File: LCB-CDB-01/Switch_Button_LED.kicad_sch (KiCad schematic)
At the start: 65 parts, among them J1 Conn_01x02, J10 Conn_01x02, J11 Conn_01x02, J12 Conn_01x02, J13 Conn_01x02, J14 Conn_01x02, J15 Conn_01x02, J16 Conn_01x02, J17 Conn_01x02, J18 Conn_01x02, J19 Conn_01x02, J2 Conn_01x02, J20 Conn_01x02, J21 Conn_01x02, J22 Conn_01x02, J23 Conn_01x02, J24 Conn_01x02, J25 Conn_01x02, J26 Conn_01x02, J27 Conn_01x02, J28 Conn_01x02, J29 Conn_01x02, J3 Conn_01x02, J30 Conn_01x02, J4 Conn_01x02, J5 Conn_01x02, J6 Conn_01x02, J7 Conn_01x02, J8 Conn_01x02, J9 Conn_01x02

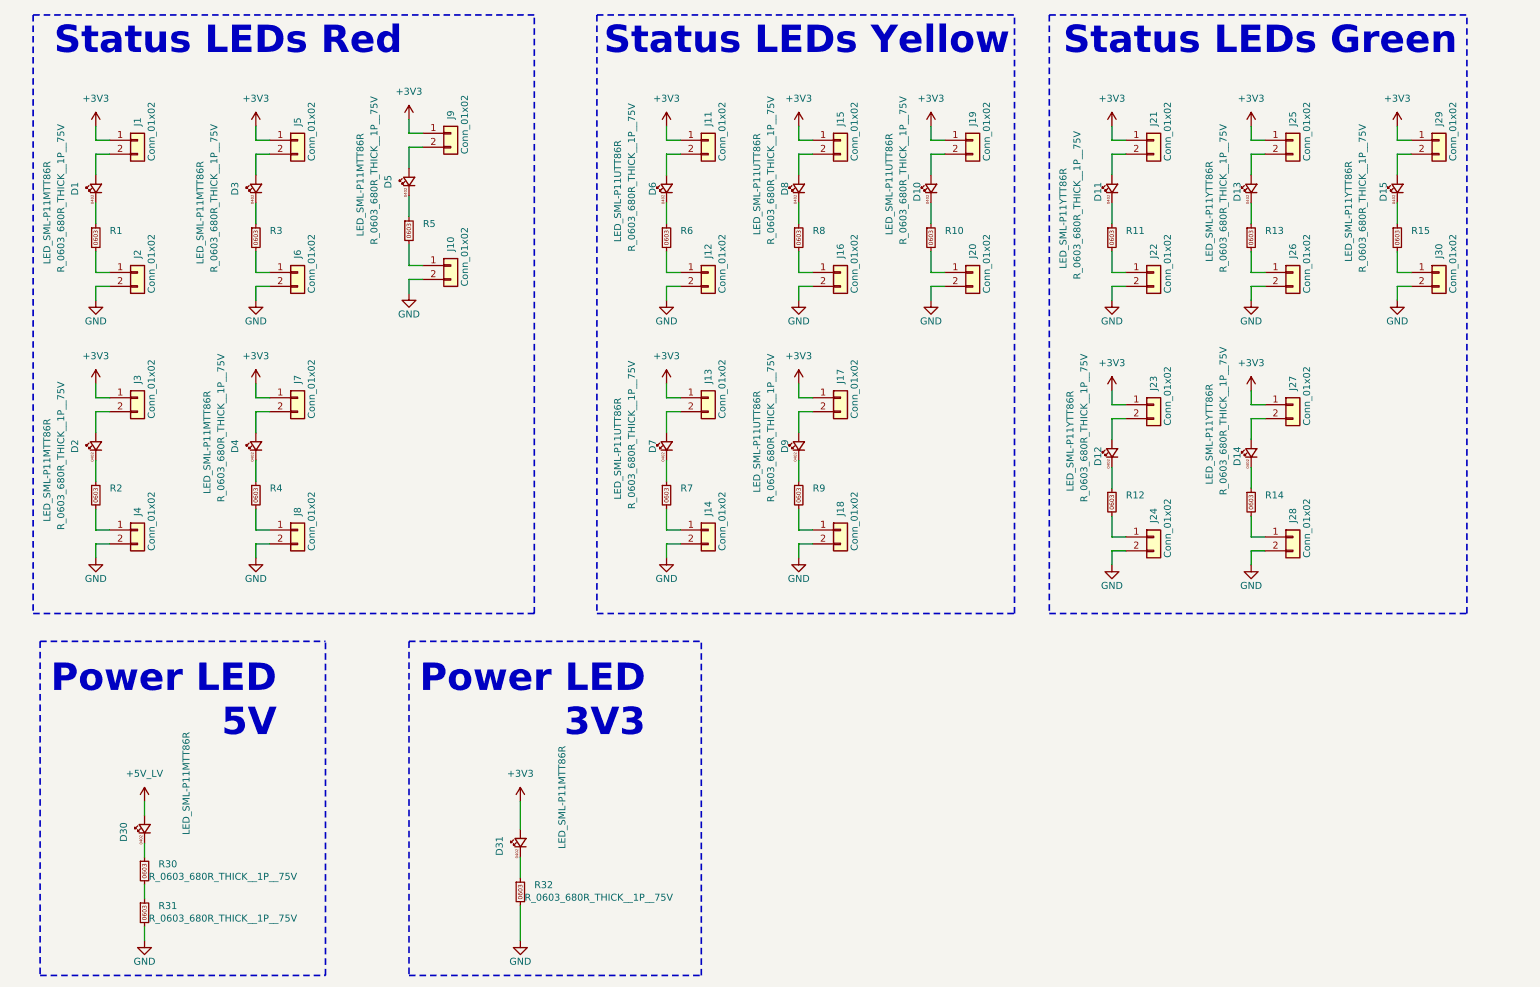
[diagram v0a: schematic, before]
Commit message: update some Rs and Cs names and values, as they can be separate values in KiCad7
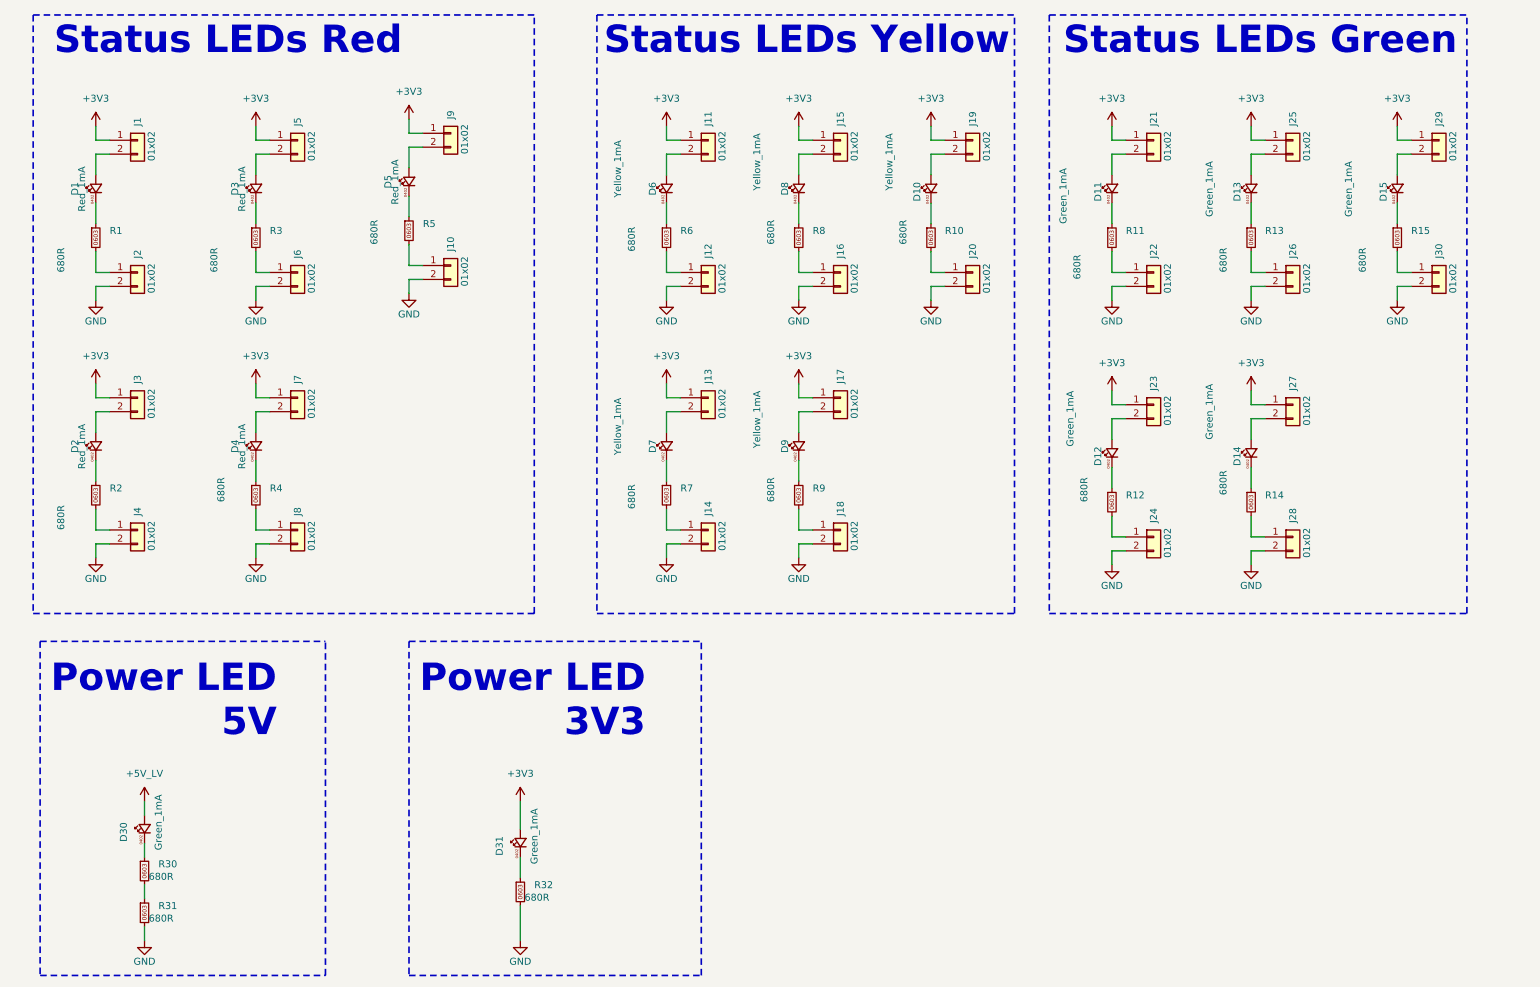
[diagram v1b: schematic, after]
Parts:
- D1, D2, D3, D4, D5: value LED_SML-P11MTT86R -> Red_1mA; symbol LEA_SymbolLibrary:LED_0402_Y_1mA_SML-P11YTT86R -> LEA_SymbolLibrary:LED_0402_R_1mA_SML-P11UTT86R; manf# SML-P11YTT86R -> SML-P11UTT86R; mouser# 755-SML-P11YTT86R -> 755-SML-P11UTT86R
- D10, D6, D7, D8, D9: value LED_SML-P11UTT86R -> Yellow_1mA
- D11, D12, D13, D14, D15: value LED_SML-P11YTT86R -> Green_1mA
- D30, D31: value LED_SML-P11MTT86R -> Green_1mA
- J1, J10, J11, J12, J13, J14, J15, J16, J17, J18, J19, J2, J20, J21, J22, J23, J24, J25, J26, J27, J28, J29, J3, J30, J4, J5, J6, J7, J8, J9: value Conn_01x02 -> 01x02
- R1, R10, R11, R12, R13, R14, R15, R2, R3, R30, R31, R32, R4, R5, R6, R7, R8, R9: value R_0603_680R_THICK__1P__75V -> 680R

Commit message: bump version to 1.1.0
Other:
- title: LCB-CBD-001: Dock -> LCB-CBD-01: Dock
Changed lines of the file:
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@@
   (paper "A4")
   (title_block
-    (title "LCB-CBD-001: Dock")
-    (date "2022-08-12")
-    (rev "0.1")
+    (title "LCB-CBD-01: Dock")
+    (date "2023-04-13")
+    (rev "1.1.0")
     (company "PADERBORN UNIVERSITY DEPARTMENT OF POWER ELECTRONICS AND ELECTRICAL DRIVES")
   )
@@
   (symbol (lib_id "LEA_SymbolLibrary:R_0603_680R_THICK__1P__75V") (at 135.89 55.88 0) (unit 1)
     (in_bom yes) (on_board yes) (dnp no)
-    (property "Reference" "R6" (at 138.43 54.61 0)
+    (property "Reference" "R6" (at 137.16 54.61 0)
       (effects (font (size 1.27 1.27)) (justify left))
     )
-    (property "Value" "680R" (at 129.54 58.42 90)
+    (property "Value" "680R" (at 133.35 58.42 90)
       (effects (font (size 1.27 1.27)) (justify left))
     )
@@
   (symbol (lib_id "LEA_SymbolLibrary:LED_0402_R_1mA_SML-P11UTT86R") (at 60.96 46.99 90) (unit 1)
     (in_bom yes) (on_board yes) (dnp no)
-    (property "Reference" "D3" (at 57.15 45.72 0)
+    (property "Reference" "D3" (at 55.88 45.72 0)
       (effects (font (size 1.27 1.27)) (justify right))
     )
@@
       (effects (font (size 1.27 1.27)) (justify left))
     )
-    (property "Value" "680R" (at 212.09 104.14 90)
+    (property "Value" "680R" (at 214.63 106.68 90)
       (effects (font (size 1.27 1.27)) (justify left))
     )
@@
   (symbol (lib_id "LEA_SymbolLibrary:LED_0402_R_1mA_SML-P11UTT86R") (at 60.96 93.98 90) (unit 1)
     (in_bom yes) (on_board yes) (dnp no)
-    (property "Reference" "D4" (at 57.15 92.71 0)
+    (property "Reference" "D4" (at 55.88 92.71 0)
       (effects (font (size 1.27 1.27)) (justify right))
     )
@@
       (effects (font (size 1.27 1.27)) (justify left))
     )
-    (property "Value" "680R" (at 262.89 62.23 90)
+    (property "Value" "680R" (at 266.7 58.42 90)
       (effects (font (size 1.27 1.27)) (justify left))
     )
@@
   (symbol (lib_id "LEA_SymbolLibrary:R_0603_680R_THICK__1P__75V") (at 31.75 102.87 0) (unit 1)
     (in_bom yes) (on_board yes) (dnp no)
-    (property "Reference" "R2" (at 34.29 101.6 0)
+    (property "Reference" "R2" (at 33.02 101.6 0)
       (effects (font (size 1.27 1.27)) (justify left))
     )
-    (property "Value" "680R" (at 25.4 109.22 90)
+    (property "Value" "680R" (at 29.21 105.41 90)
       (effects (font (size 1.27 1.27)) (justify left))
     )
@@
       (effects (font (size 1.27 1.27)) (justify right))
     )
-    (property "Value" "Green_1mA" (at 234.95 41.91 0)
+    (property "Value" "Green_1mA" (at 237.49 41.91 0)
       (effects (font (size 1.27 1.27)) (justify right))
     )
@@
   (symbol (lib_id "LEA_SymbolLibrary:LED_0402_R_1mA_SML-P11UTT86R") (at 31.75 46.99 90) (unit 1)
     (in_bom yes) (on_board yes) (dnp no)
-    (property "Reference" "D1" (at 27.94 45.72 0)
+    (property "Reference" "D1" (at 26.67 45.72 0)
       (effects (font (size 1.27 1.27)) (justify right))
     )
@@
       (effects (font (size 1.27 1.27)) (justify left))
     )
-    (property "Value" "680R" (at 237.49 62.23 90)
+    (property "Value" "680R" (at 240.03 58.42 90)
       (effects (font (size 1.27 1.27)) (justify left))
     )
@@
       (effects (font (size 1.27 1.27)) (justify right))
     )
-    (property "Value" "Yellow_1mA" (at 176.53 36.83 0)
+    (property "Value" "Yellow_1mA" (at 179.07 40.64 0)
       (effects (font (size 1.27 1.27)) (justify right))
     )
@@
       (effects (font (size 1.27 1.27)) (justify right))
     )
-    (property "Value" "Yellow_1mA" (at 127 38.1 0)
+    (property "Value" "Yellow_1mA" (at 130.81 41.91 0)
       (effects (font (size 1.27 1.27)) (justify right))
     )
@@
       (effects (font (size 1.27 1.27)) (justify right))
     )
-    (property "Value" "Yellow_1mA" (at 127 85.09 0)
+    (property "Value" "Yellow_1mA" (at 130.81 87.63 0)
       (effects (font (size 1.27 1.27)) (justify right))
     )
@@
       (effects (font (size 1.27 1.27)) (justify right))
     )
-    (property "Value" "Green_1mA" (at 208.28 43.18 0)
+    (property "Value" "Green_1mA" (at 212.09 43.18 0)
       (effects (font (size 1.27 1.27)) (justify right))
     )
@@
       (effects (font (size 1.27 1.27)) (justify right))
     )
-    (property "Value" "Yellow_1mA" (at 152.4 83.82 0)
+    (property "Value" "Yellow_1mA" (at 154.94 87.63 0)
       (effects (font (size 1.27 1.27)) (justify right))
     )
@@
   (symbol (lib_id "LEA_SymbolLibrary:R_0603_680R_THICK__1P__75V") (at 60.96 55.88 0) (unit 1)
     (in_bom yes) (on_board yes) (dnp no)
-    (property "Reference" "R3" (at 63.5 54.61 0)
+    (property "Reference" "R3" (at 62.23 55.88 0)
       (effects (font (size 1.27 1.27)) (justify left))
     )
-    (property "Value" "680R" (at 53.34 62.23 90)
+    (property "Value" "680R" (at 58.42 58.42 90)
       (effects (font (size 1.27 1.27)) (justify left))
     )
@@
       (effects (font (size 1.27 1.27)) (justify left))
     )
-    (property "Value" "680R" (at 179.07 57.15 90)
+    (property "Value" "680R" (at 181.61 58.42 90)
       (effects (font (size 1.27 1.27)) (justify left))
     )
@@
   (symbol (lib_id "LEA_SymbolLibrary:LED_0402_R_1mA_SML-P11UTT86R") (at 88.9 45.72 90) (unit 1)
     (in_bom yes) (on_board yes) (dnp no)
-    (property "Reference" "D5" (at 85.09 44.45 0)
+    (property "Reference" "D5" (at 83.82 44.45 0)
       (effects (font (size 1.27 1.27)) (justify right))
     )
@@
       (effects (font (size 1.27 1.27)) (justify left))
     )
-    (property "Value" "680R" (at 210.82 63.5 90)
+    (property "Value" "680R" (at 214.63 58.42 90)
       (effects (font (size 1.27 1.27)) (justify left))
     )
@@
       (effects (font (size 1.27 1.27)) (justify left))
     )
-    (property "Value" "680R" (at 129.54 105.41 90)
+    (property "Value" "680R" (at 133.35 105.41 90)
       (effects (font (size 1.27 1.27)) (justify left))
     )
@@
       (effects (font (size 1.27 1.27)) (justify right))
     )
-    (property "Value" "Yellow_1mA" (at 152.4 36.83 0)
+    (property "Value" "Yellow_1mA" (at 153.67 40.64 0)
       (effects (font (size 1.27 1.27)) (justify right))
     )
@@
       (effects (font (size 1.27 1.27)) (justify right))
     )
-    (property "Value" "Green_1mA" (at 209.55 83.82 0)
+    (property "Value" "Green_1mA" (at 212.09 90.17 0)
       (effects (font (size 1.27 1.27)) (justify right))
     )
@@
   (symbol (lib_id "LEA_SymbolLibrary:R_0603_680R_THICK__1P__75V") (at 160.02 55.88 0) (unit 1)
     (in_bom yes) (on_board yes) (dnp no)
-    (property "Reference" "R8" (at 162.56 54.61 0)
+    (property "Reference" "R8" (at 161.29 54.61 0)
       (effects (font (size 1.27 1.27)) (justify left))
     )
-    (property "Value" "680R" (at 154.94 57.15 90)
+    (property "Value" "680R" (at 157.48 58.42 90)
       (effects (font (size 1.27 1.27)) (justify left))
     )
@@
       (effects (font (size 1.27 1.27)) (justify left))
     )
-    (property "Value" "680R" (at 54.61 104.14 90)
+    (property "Value" "680R" (at 58.42 105.41 90)
       (effects (font (size 1.27 1.27)) (justify left))
     )
@@
       (effects (font (size 1.27 1.27)) (justify left))
     )
-    (property "Value" "680R" (at 154.94 104.14 90)
+    (property "Value" "680R" (at 157.48 105.41 90)
       (effects (font (size 1.27 1.27)) (justify left))
     )
@@
       (effects (font (size 1.27 1.27)) (justify right))
     )
-    (property "Value" "Green_1mA" (at 260.35 41.91 0)
+    (property "Value" "Green_1mA" (at 264.16 41.91 0)
       (effects (font (size 1.27 1.27)) (justify right))
     )
@@
   (symbol (lib_id "LEA_SymbolLibrary:R_0603_680R_THICK__1P__75V") (at 88.9 54.61 0) (unit 1)
     (in_bom yes) (on_board yes) (dnp no)
-    (property "Reference" "R5" (at 91.44 53.34 0)
+    (property "Reference" "R5" (at 90.17 54.61 0)
       (effects (font (size 1.27 1.27)) (justify left))
     )
-    (property "Value" "680R" (at 82.55 57.15 90)
+    (property "Value" "680R" (at 86.36 57.15 90)
       (effects (font (size 1.27 1.27)) (justify left))
     )
@@
   (symbol (lib_id "LEA_SymbolLibrary:R_0603_680R_THICK__1P__75V") (at 31.75 55.88 0) (unit 1)
     (in_bom yes) (on_board yes) (dnp no)
-    (property "Reference" "R1" (at 34.29 54.61 0)
+    (property "Reference" "R1" (at 33.02 55.88 0)
       (effects (font (size 1.27 1.27)) (justify left))
     )
-    (property "Value" "680R" (at 25.4 62.23 90)
+    (property "Value" "680R" (at 29.21 58.42 90)
       (effects (font (size 1.27 1.27)) (justify left))
     )
@@
   (symbol (lib_id "LEA_SymbolLibrary:LED_0402_R_1mA_SML-P11UTT86R") (at 31.75 93.98 90) (unit 1)
     (in_bom yes) (on_board yes) (dnp no)
-    (property "Reference" "D2" (at 27.94 92.71 0)
+    (property "Reference" "D2" (at 26.67 92.71 0)
       (effects (font (size 1.27 1.27)) (justify right))
     )
@@
       (effects (font (size 1.27 1.27)) (justify right))
     )
-    (property "Value" "Green_1mA" (at 234.95 82.55 0)
+    (property "Value" "Green_1mA" (at 237.49 90.17 0)
       (effects (font (size 1.27 1.27)) (justify right))
     )
@@
       (effects (font (size 1.27 1.27)) (justify left))
     )
-    (property "Value" "680R" (at 237.49 102.87 90)
+    (property "Value" "680R" (at 240.03 106.68 90)
       (effects (font (size 1.27 1.27)) (justify left))
     )

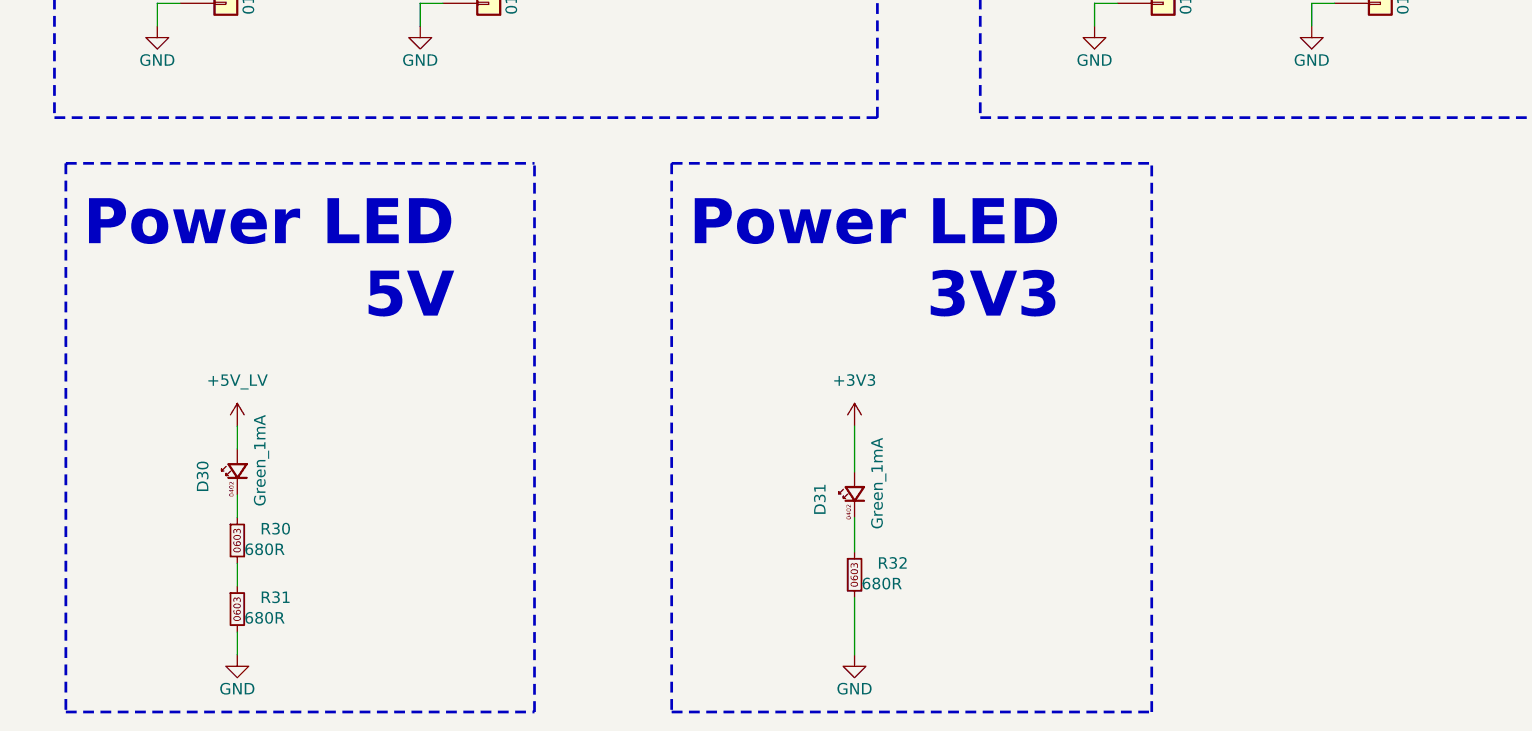
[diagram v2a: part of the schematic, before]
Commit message: update: Issue fix - 3V supply for potentiometers
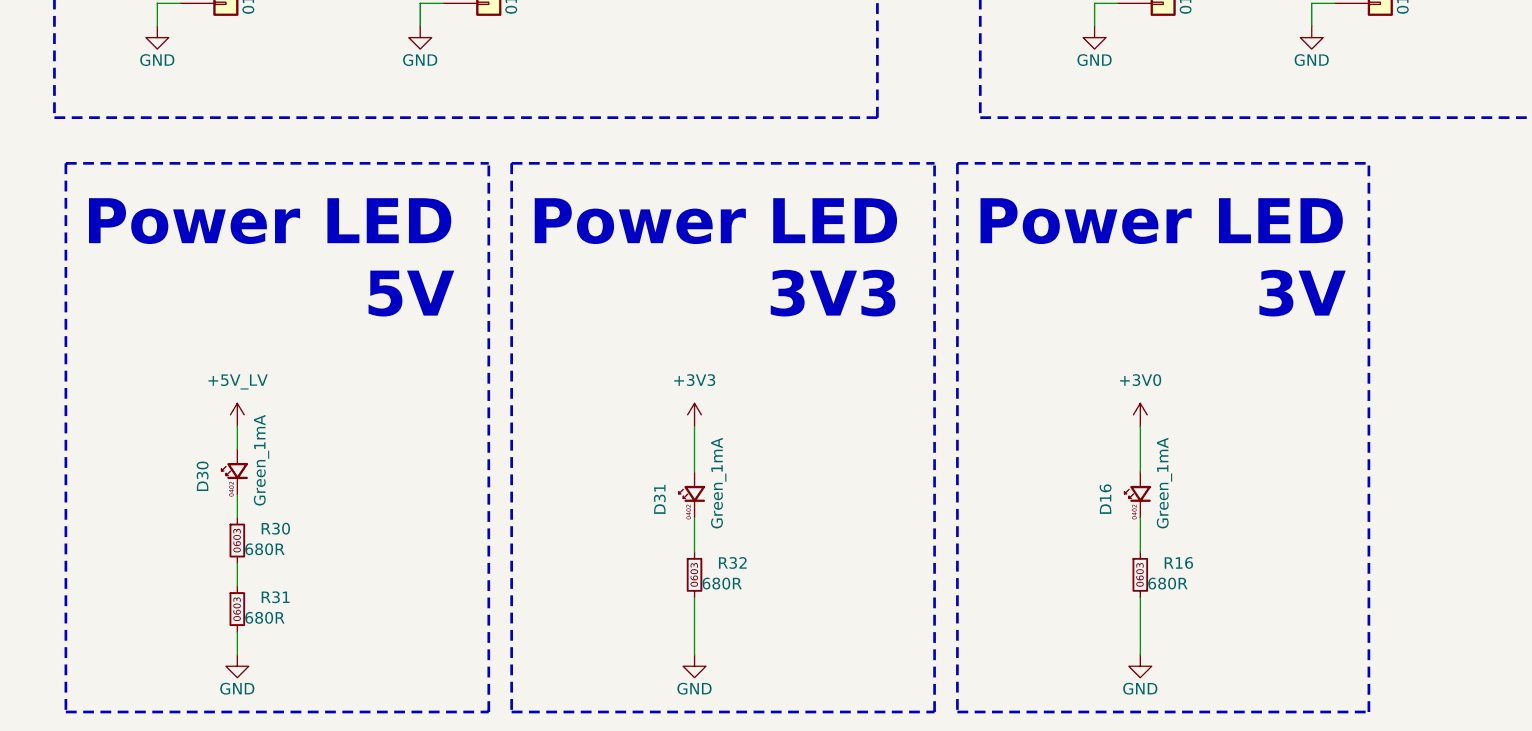
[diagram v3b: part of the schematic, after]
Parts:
- added D16: Green_1mA, LEA_FootprintLibrary:LED_0402, symbol LEA_SymbolLibrary:LED_0402_G_1mA_SML-P11MTT86R
- added R16: 680R, LEA_FootprintLibrary:R_0603, symbol LEA_SymbolLibrary:R_0603_680R_THICK__1P__75V
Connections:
- net GND: now also R16.2
- new net: D16.C, R16.1
- new net +3V0: D16.A
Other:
- note added: "Power LED 3V"
- moved on the sheet: D31, R32

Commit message: version 1.2.0
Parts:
- D1, D2, D3, D4, D5: footprint LEA_FootprintLibrary:LED_0402 -> LEA_FootprintLibrary:LED_0402_R
- D10, D6, D7, D8, D9: footprint LEA_FootprintLibrary:LED_0402 -> LEA_FootprintLibrary:LED_0402_Y
- D11, D12, D13, D14, D15, D16, D30, D31: footprint LEA_FootprintLibrary:LED_0402 -> LEA_FootprintLibrary:LED_0402_G

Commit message: update symbols without simulation models
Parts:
- D1, D16, D2, D3, D30, D31, D4, D5: Mfr. No SML-P11MTT86R -> (none); Mouser No 755-SML-P11MTT86R -> (none)
- D10, D6, D7, D8, D9: Mfr. No SML-P11UTT86R -> (none); Mouser No 755-SML-P11UTT86R -> (none)
- D11, D12, D13, D14, D15: Mfr. No SML-P11YTT86R -> (none); Mouser No 755-SML-P11YTT86R -> (none)
- J1, J10, J11, J12, J13, J14, J15, J16, J17, J18, J19, J2, J20, J21, J22, J23, J24, J25, J26, J27, J28, J29, J3, J30, J4, J5, J6, J7, J8, J9: Mouser No. 855-M20-9990245 -> (none)
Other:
- title: LCB-CBD-01: Dock -> LCB-CDB-01: Dock Board
